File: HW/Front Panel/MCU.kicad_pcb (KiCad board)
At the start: 2 copper layers, 150 x 50 mm, 44 parts, among them J1 CTRL, J10 SPI, J11 EXT_PWM, J12 EXT_PWM_DUAL, J13 1Wire, J14 JUMPER, J15 JUMPER, J16 JUMPER, J17 JUMPER, J18 ENC_SW_SEL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

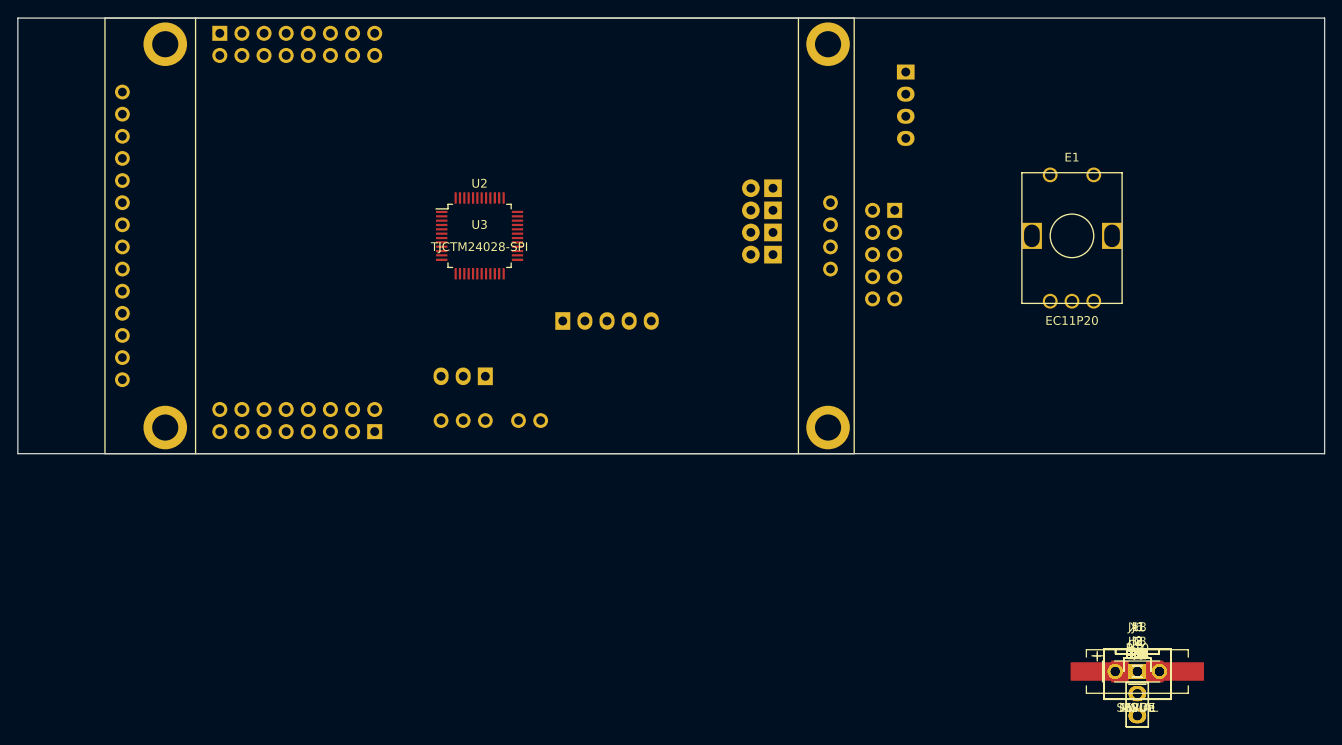
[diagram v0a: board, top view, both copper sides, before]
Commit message: Front Panel PCB added. Unfinished - just for transfer
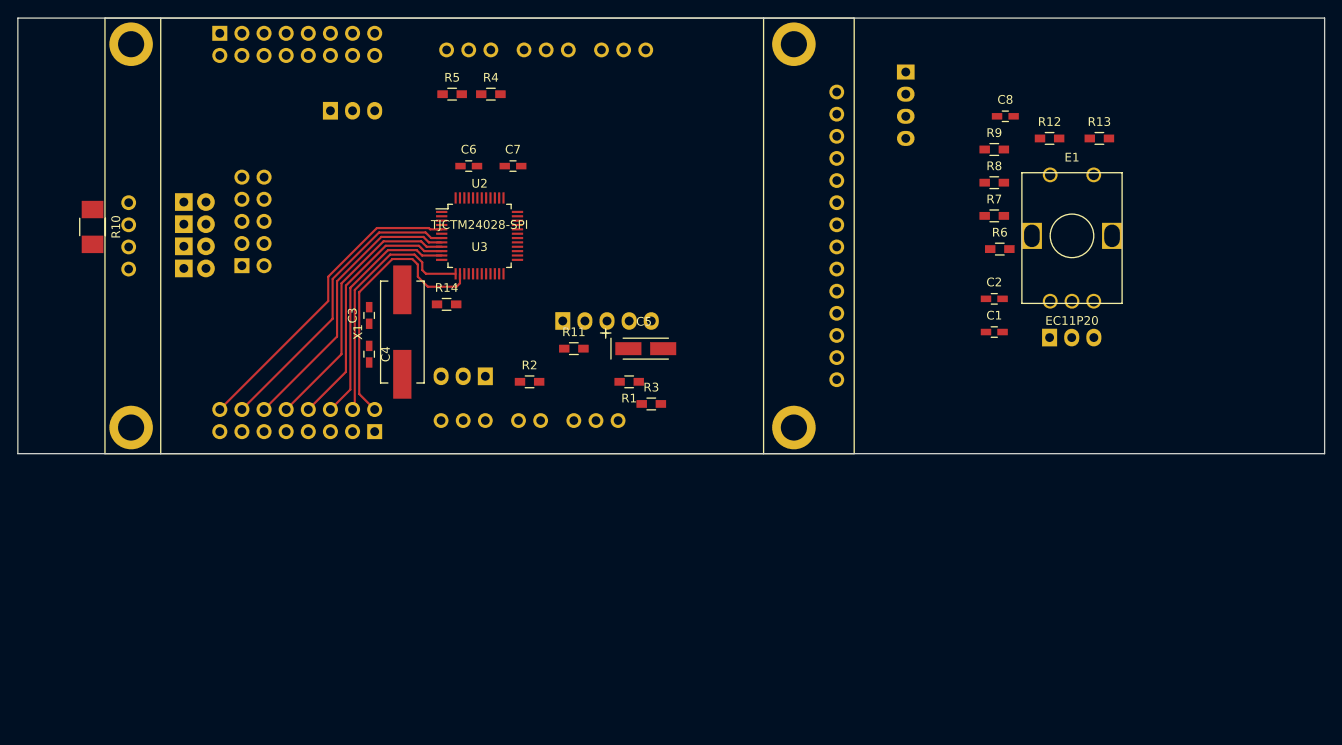
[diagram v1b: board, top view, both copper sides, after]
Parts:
- J13, J18, J2, J3, J6, J8: moved to B.Cu
- moved R10 130.3 mm to (28.6, 54.0), turned to 270 degrees
- moved J6 112.8 mm to (55.9, 40.6), turned to 270 degrees
- moved J2 104.8 mm to (71.8, 33.7)
- moved R5 102.8 mm to (69.8, 38.7)
- moved R4 99.5 mm to (74.3, 38.7)
- moved J8 98.5 mm to (80.6, 33.7)
- moved C3 97.2 mm to (60.3, 64.1), turned to 90 degrees
- moved C6 96.2 mm to (71.8, 47.0)
- moved C4 95.4 mm to (60.3, 68.6), turned to 270 degrees
- moved X1 92.9 mm to (64.1, 66.0), turned to 90 degrees
- moved J13 92.6 mm to (89.5, 33.7)
- moved C7 92.2 mm to (76.8, 47.0)
- moved R14 89.8 mm to (69.2, 62.9)
- moved R2 77.3 mm to (78.7, 71.8)
- moved J10 75.2 mm to (45.7, 58.4), turned to 0 degrees
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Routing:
- net PP0: track 0.00 -> 35.8 mm
- net PP1: track 0.00 -> 34.3 mm
- net PP2: track 0.00 -> 32.6 mm
- net PP3: track 0.00 -> 30.9 mm
- net PP7: track 0.00 -> 30.7 mm
- net PP4: track 0.00 -> 29.2 mm
- net PP6: track 0.00 -> 28.5 mm
- net PP5: track 0.00 -> 27.4 mm

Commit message: Front Panel Schematic v1.01 + PCB design added
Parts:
- added MNT_HOLE_3: Val**, suf_mounting:MNT_HOLE_3, F.Cu at (147.0, 77.0)
- added MNT_HOLE_3: Val**, suf_mounting:MNT_HOLE_3, F.Cu at (147.0, 33.0)
- J9: value CTRL -> EXT_IO
- moved R10 82.0 mm to (110.5, 57.1), turned to 90 degrees
- moved C2 51.1 mm to (84.5, 43.8)
- moved R6 49.5 mm to (84.5, 45.7)
- moved C1 48.5 mm to (88.0, 45.7), turned to 90 degrees
- moved R7 45.8 mm to (86.4, 49.5)
- moved R9 41.9 mm to (90.2, 44.5), turned to 270 degrees
- moved R8 39.5 mm to (92.7, 45.7), turned to 270 degrees
- moved R13 24.4 mm to (125.1, 59.1), turned to 180 degrees
- moved C8 23.0 mm to (123.8, 62.2), turned to 270 degrees
- moved R11 19.0 mm to (101.0, 76.2), turned to 90 degrees
- moved J18 18.5 mm to (120.7, 61.6), turned to 0 degrees
- moved C5 11.0 mm to (102.9, 69.8)
- moved J4 11.0 mm to (93.3, 66.7)
- moved C3 10.8 mm to (69.8, 69.2)
- moved C4 10.8 mm to (69.8, 73.7)
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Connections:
- J12 pad 2: PWM_3 -> Net-(J11-Pad2)
- J12 pad 3: Net-(J11-Pad2) -> PWM_3
- J6 pad 2: PWM_1 -> Net-(J1-Pad14)
- J6 pad 3: Net-(J1-Pad14) -> PWM_1
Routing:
- net VCC: track 0.00 -> 337.3 mm
- net RPM_IN: track 0.00 -> 83.8 mm, vias 0 -> 1
- net GNDA: track 0.00 -> 78.4 mm
- net Net-(E1-Pad2): track 0.00 -> 77.7 mm
- net CAL: track 0.00 -> 71.9 mm, vias 0 -> 1
- net Net-(E1-Pad3): track 0.00 -> 65.3 mm
- net TFT_CS: track 0.00 -> 60.1 mm
- net SPINDLE_SPEED: track 0.00 -> 58.6 mm, vias 0 -> 3
- net TFT_DC: track 0.00 -> 54.8 mm, vias 0 -> 1
- net TFT_RST: track 0.00 -> 54.3 mm, vias 0 -> 1
- net TICECLK: track 0.00 -> 54.0 mm
- net SPINDLE_SWITCH: track 0.00 -> 52.9 mm, vias 0 -> 1
- net Net-(E1-Pad4): track 0.00 -> 51.0 mm
- net TFT_MOSI: track 0.00 -> 48.6 mm
- net TICERST: track 0.00 -> 48.4 mm, vias 0 -> 1
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- added copper zone on B.Cu, net GND
- added copper zone on F.Cu, net GND
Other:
- board size 150 x 50 mm -> 120 x 50 mm

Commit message: Front Panel SW added - WIP
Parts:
- added REF**: Symbol_OSHW-Logo_SilkScreen, Symbols:Symbol_OSHW-Logo_SilkScreen, B.Cu at (100.0, 38.0)
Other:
- board text added: "CNC Motor Driver Front Panel v1.01 Designed by SUF"
